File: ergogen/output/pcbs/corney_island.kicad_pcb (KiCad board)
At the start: 2 copper layers, 133.8 x 91.7 mm, 73 parts

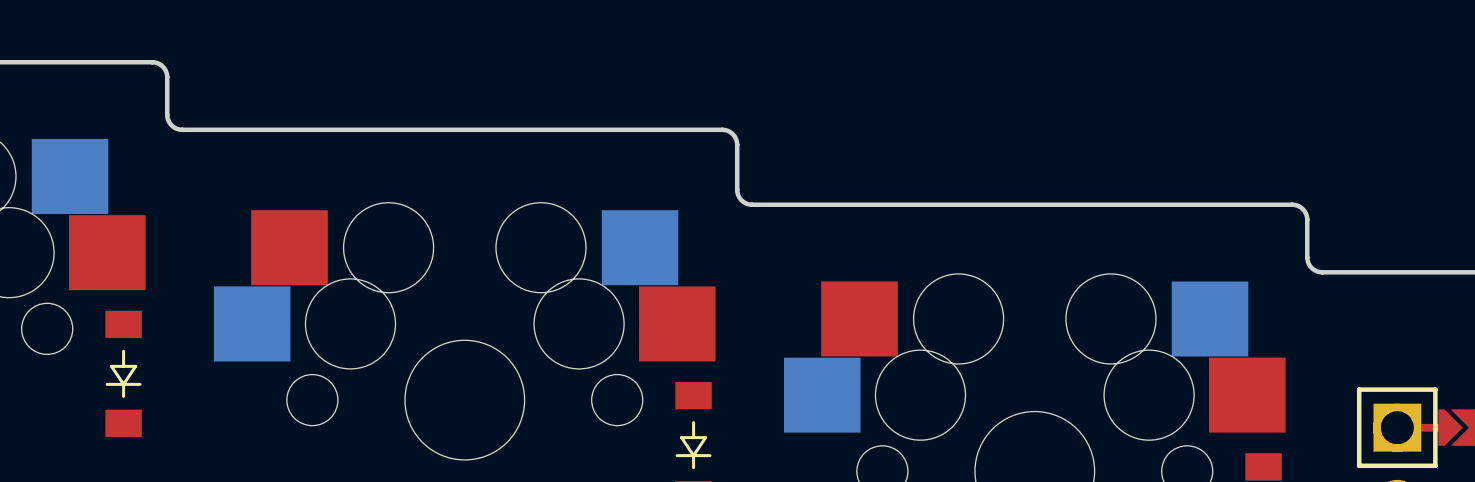
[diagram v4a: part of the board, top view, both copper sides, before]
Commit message: Add missing parametric measures
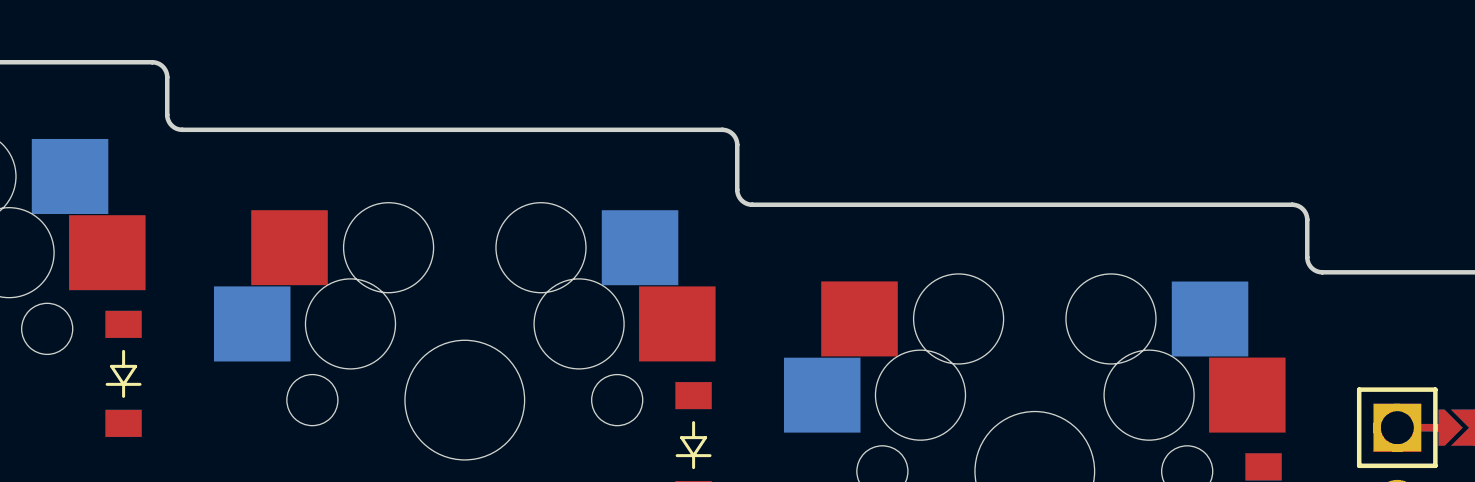
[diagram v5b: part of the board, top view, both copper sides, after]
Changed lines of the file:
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@@
 (gr_line (start 148.58 45.988) (end 165.582 45.988) (angle 90) (layer Edge.Cuts) (width 0.15))
 (gr_line (start 166.082 46.488) (end 166.082 47.74) (angle 90) (layer Edge.Cuts) (width 0.15))
-(gr_line (start 166.582 48.24) (end 184.581 48.24) (angle 90) (layer Edge.Cuts) (width 0.15))
-(gr_line (start 185.081 48.74) (end 185.081 50.238) (angle 90) (layer Edge.Cuts) (width 0.15))
-(gr_line (start 185.581 50.738) (end 203.58222192628773 50.738) (angle 90) (layer Edge.Cuts) (width 0.15))
+(gr_line (start 166.582 48.24) (end 184.582 48.24) (angle 90) (layer Edge.Cuts) (width 0.15))
+(gr_line (start 185.082 48.74) (end 185.082 50.238) (angle 90) (layer Edge.Cuts) (width 0.15))
+(gr_line (start 185.582 50.738) (end 203.58222192628773 50.738) (angle 90) (layer Edge.Cuts) (width 0.15))
 (gr_line (start 204.08222192628773 51.23777800000971) (end 204.08277807371226 52.49022199999308) (angle 90) (layer Edge.Cuts) (width 0.15))
 (gr_line (start 224.518 113.996596) (end 210.97353193043912 137.45836746290388) (angle 90) (layer Edge.Cuts) (width 0.15))
@@
 (gr_arc (start 165.582 46.488) (end 166.082 46.488) (angle -90) (layer Edge.Cuts) (width 0.15))
 (gr_arc (start 166.582 47.74) (end 166.082 47.74) (angle -90) (layer Edge.Cuts) (width 0.15))
-(gr_arc (start 184.581 48.74) (end 185.081 48.74) (angle -90) (layer Edge.Cuts) (width 0.15))
-(gr_arc (start 185.581 50.238) (end 185.081 50.238) (angle -90) (layer Edge.Cuts) (width 0.15))
+(gr_arc (start 184.582 48.74) (end 185.082 48.74) (angle -90) (layer Edge.Cuts) (width 0.15))
+(gr_arc (start 185.582 50.238) (end 185.082 50.238) (angle -90) (layer Edge.Cuts) (width 0.15))
 (gr_arc (start 203.58222192628773 51.238) (end 204.08222192628773 51.237778) (angle -89.97456067668081) (layer Edge.Cuts) (width 0.15))
 (gr_arc (start 204.58277807371226 52.48999999999069) (end 204.08277807371226 52.49022199999069) (angle -89.97456067529339) (layer Edge.Cuts) (width 0.15))

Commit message: Refresh generated files.
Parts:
- D1, D10, D11, D12, D13, D14, D15, D16, D17, D18, D19, D2, D20, D21, D3, D4, D5, D6, D7, D8, D9: moved to B.Cu
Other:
- outline, holes or cut-outs redrawn

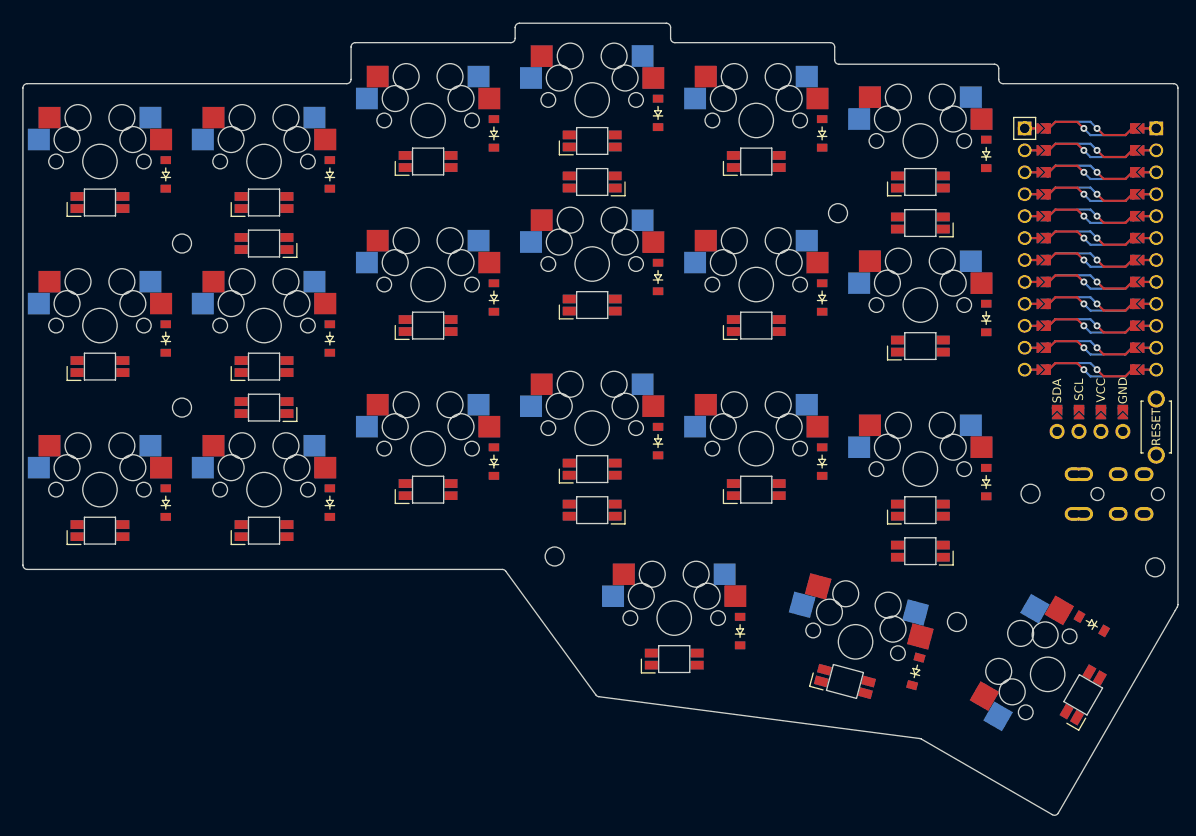
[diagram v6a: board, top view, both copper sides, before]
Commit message: Split diode position on F and B layers
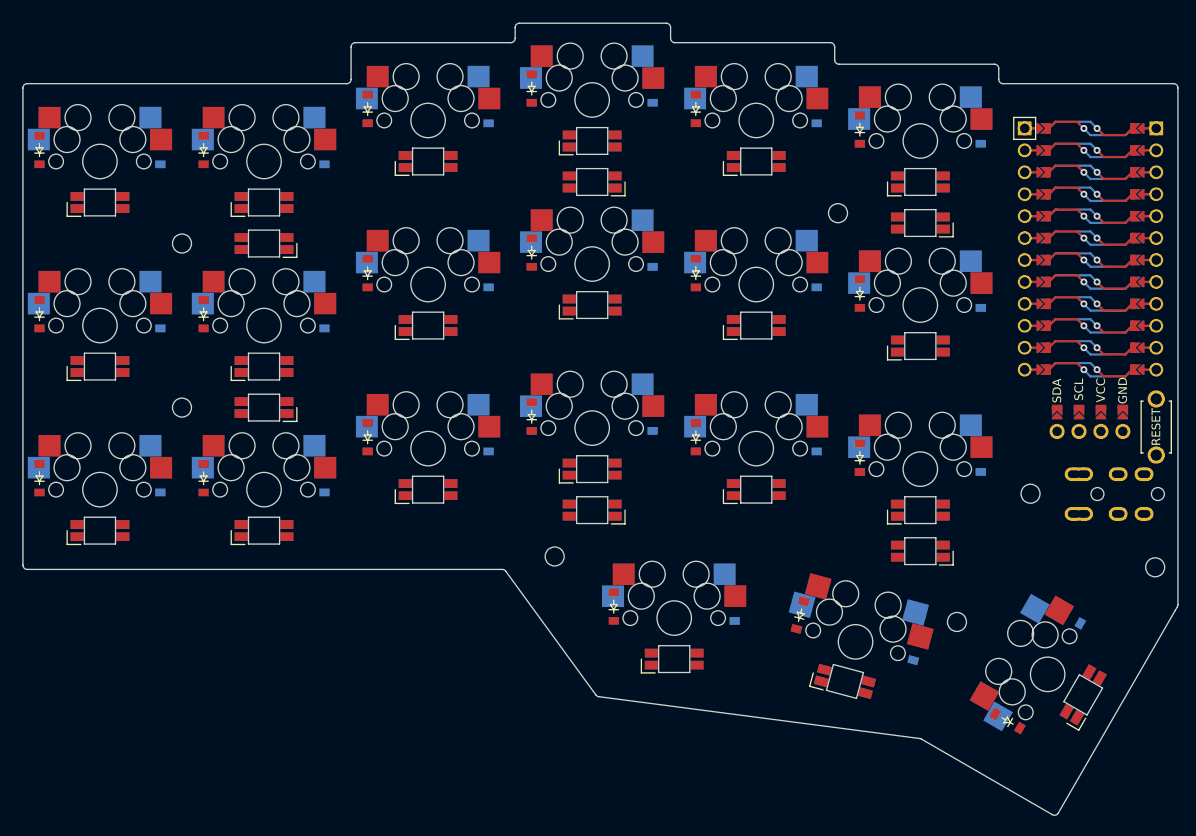
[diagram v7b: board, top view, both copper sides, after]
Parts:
- added D22: , ComboDiode, F.Cu at (93.0, 98.7)
- added D23: , ComboDiode, F.Cu at (93.0, 79.7)
- added D24: , ComboDiode, F.Cu at (93.0, 60.7)
- added D25: , ComboDiode, F.Cu at (112.0, 98.7)
- added D26: , ComboDiode, F.Cu at (112.0, 79.7)
- added D27: , ComboDiode, F.Cu at (112.0, 60.7)
- added D28: , ComboDiode, F.Cu at (131.0, 93.9)
- added D29: , ComboDiode, F.Cu at (131.0, 74.9)
- added D30: , ComboDiode, F.Cu at (131.0, 55.9)
- added D31: , ComboDiode, F.Cu at (150.0, 91.5)
- added D32: , ComboDiode, F.Cu at (150.0, 72.5)
- added D33: , ComboDiode, F.Cu at (150.0, 53.5)
- added D34: , ComboDiode, F.Cu at (169.0, 93.9)
- added D35: , ComboDiode, F.Cu at (169.0, 74.9)
- added D36: , ComboDiode, F.Cu at (169.0, 55.9)
- added D37: , ComboDiode, F.Cu at (188.0, 96.3)
- added D38: , ComboDiode, F.Cu at (188.0, 77.3)
- added D39: , ComboDiode, F.Cu at (188.0, 58.3)
- added D40: , ComboDiode, F.Cu at (159.5, 113.5)
- added D41: , ComboDiode, F.Cu at (181.1, 114.5)
- added D42: , ComboDiode, F.Cu at (205.1, 126.8)
- B1: footprint kbd:ResetSW -> corne_reset_switch
- moved D21 2.89 mm to (212.1, 114.7)
- moved D10 2.89 mm to (164.0, 91.5)
- moved D11 2.89 mm to (164.0, 72.5)
- moved D12 2.89 mm to (164.0, 53.5)
- moved D13 2.89 mm to (183.0, 93.9)
- moved D14 2.89 mm to (183.0, 74.9)
- moved D15 2.89 mm to (183.0, 55.9)
- moved D16 2.89 mm to (202.0, 96.3)
- moved D17 2.89 mm to (202.0, 77.3)
- moved D18 2.89 mm to (202.0, 58.3)
- moved D19 2.89 mm to (173.5, 113.5)
- moved D7 2.89 mm to (145.0, 93.9)
- moved D8 2.89 mm to (145.0, 74.9)
- moved D9 2.89 mm to (145.0, 55.9)
- moved D1 2.89 mm to (107.0, 98.7)
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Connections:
- LED1 pad 2: LED_21 -> LED_19
- LED1 pad 4: LED_20 -> LED_18
- LED10 pad 2: ULED_3 -> ULED_4
- LED12 pad 2: ULED_2 -> ULED_3
- LED13 pad 4: ULED_5 -> LED_5
- LED15 pad 4: ULED_6 -> LED_7
- LED16 pad 2: LED_3 -> ULED_2
- LED17 pad 4: LED_1 -> ULED_1
- LED22 pad 4: ULED_0 -> ULED_6
- LED23 pad 4: ULED_1 -> ULED_5
- LED24 pad 4: (no net) -> ULED_4
- LED25 pad 4: ULED_2 -> ULED_3
- LED26 pad 2: (no net) -> LED_3
- LED26 pad 4: (no net) -> ULED_2
- LED27 pad 2: (no net) -> ULED_1
- LED27 pad 4: (no net) -> LED_1
- LED3 pad 2: LED_19 -> LED_21
- LED3 pad 4: LED_18 -> LED_20
- LED5 pad 2: ULED_0 -> ULED_6
- LED6 pad 2: ULED_1 -> ULED_5

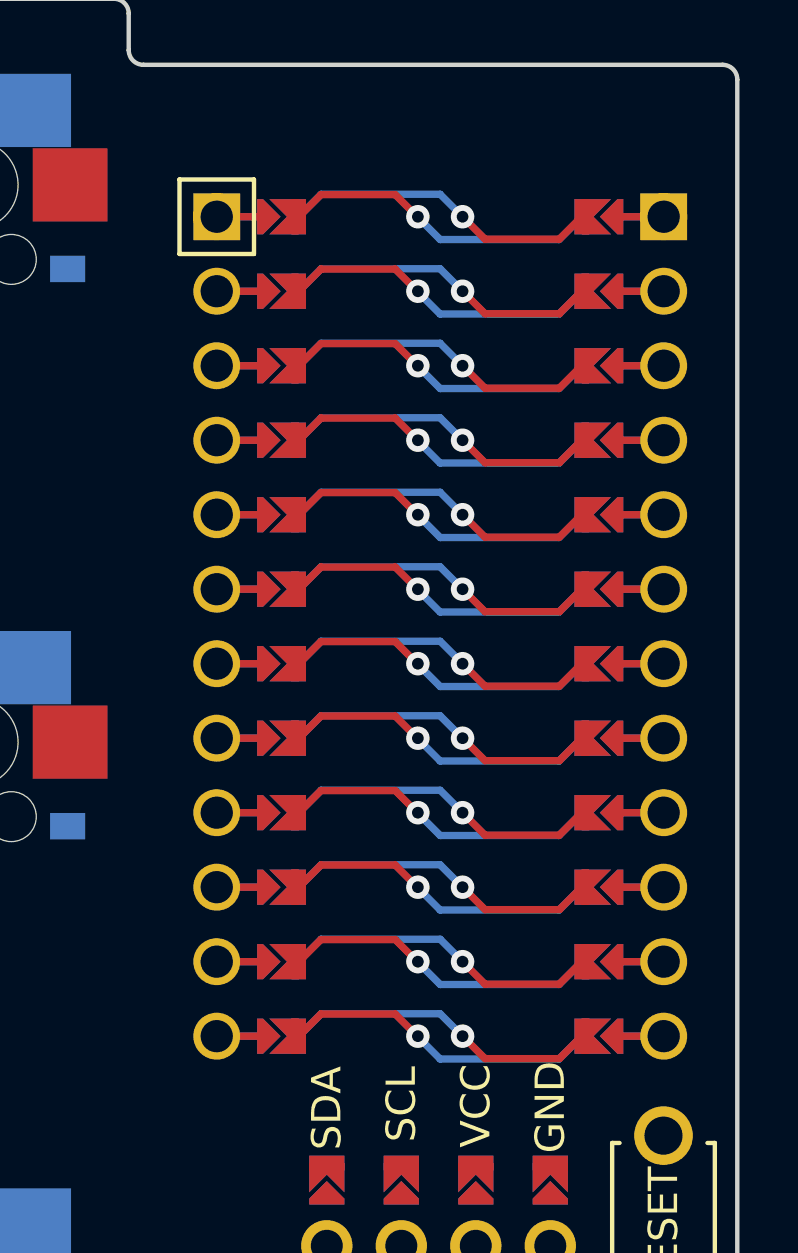
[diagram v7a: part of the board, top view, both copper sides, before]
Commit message: Switch to infused-kim nice-nano footprint
Signed-off-by: Marco Massarelli <marco.massarelli@gmail.com>
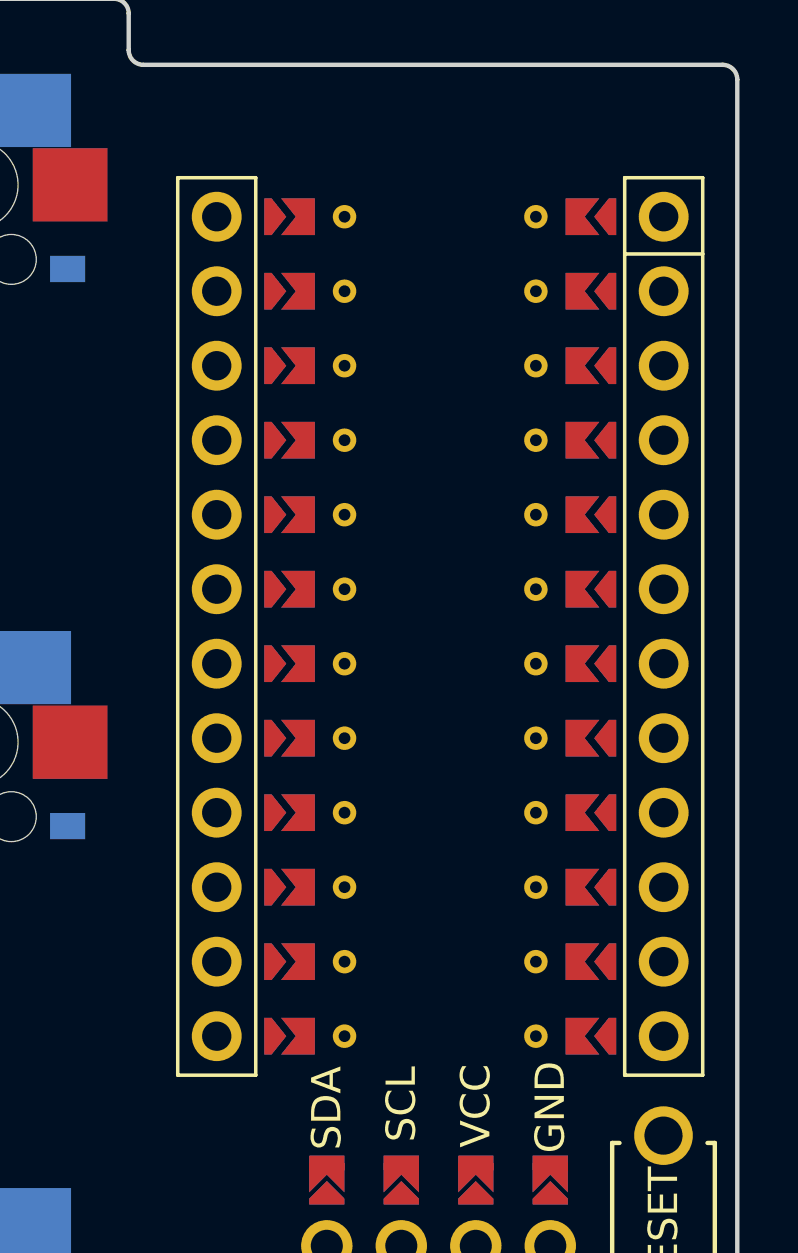
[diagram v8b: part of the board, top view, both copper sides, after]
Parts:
- MCU1: footprint ProMicro -> nice_nano
- moved MCU1 1.27 mm to (214.7, 70.9), turned to 0 degrees
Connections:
- net MOSI renamed MCU1_11
- net P10 renamed MCU1_12
- net RAW renamed MCU1_1
- MCU1 pad 10: C5 -> MCU1_10
- MCU1 pad 13: P9 -> MCU1_13
- MCU1 pad 14: R3 -> MCU1_14
- MCU1 pad 15: R2 -> MCU1_15
- MCU1 pad 16: R1 -> MCU1_16
- MCU1 pad 17: R0 -> MCU1_17
- MCU1 pad 18: CS -> MCU1_18
- MCU1 pad 19: SCL -> MCU1_19
- MCU1 pad 2: GND -> MCU1_2
- MCU1 pad 20: SDA -> MCU1_20
- MCU1 pad 21: GND -> MCU1_21
- MCU1 pad 22: GND -> MCU1_22
- MCU1 pad 23: data -> MCU1_23
- MCU1 pad 24: LED -> MCU1_24
- MCU1 pad 3: RST -> MCU1_3
- MCU1 pad 4: VCC -> MCU1_4
- MCU1 pad 5: C0 -> MCU1_5
- MCU1 pad 6: C1 -> MCU1_6
- MCU1 pad 7: C2 -> MCU1_7
- MCU1 pad 8: C3 -> MCU1_8
- MCU1 pad 9: C4 -> MCU1_9
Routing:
- net (no net): track 262.1 -> 0.00 mm
- net data: vias 1 -> 0
- net VCC: vias 1 -> 0
- net SDA: vias 1 -> 0
- net SCL: vias 1 -> 0
- net RST: vias 1 -> 0
- net R3: vias 1 -> 0
- net R2: vias 1 -> 0
- net R1: vias 1 -> 0
- net R0: vias 1 -> 0
- net P9: vias 1 -> 0
- net MCU1_12: vias 1 -> 0
- net MCU1_11: vias 1 -> 0
- net MCU1_1: vias 1 -> 0
- net LED: vias 1 -> 0
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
